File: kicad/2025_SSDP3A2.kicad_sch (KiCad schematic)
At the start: 72 parts, among them J1 SolderPad, J2 SolderPad, J3 SolderPad, J4 SolderPad, J5 SolderPad, J6 SolderPad, J7 SolderPad_01x02, J8 SolderPad_1x03, Q1 CSD19537Q3, Q2 CSD19537Q3, Q3 BSZ096N10LS5, U1 LM5050-1, U2 LM5146RGYR

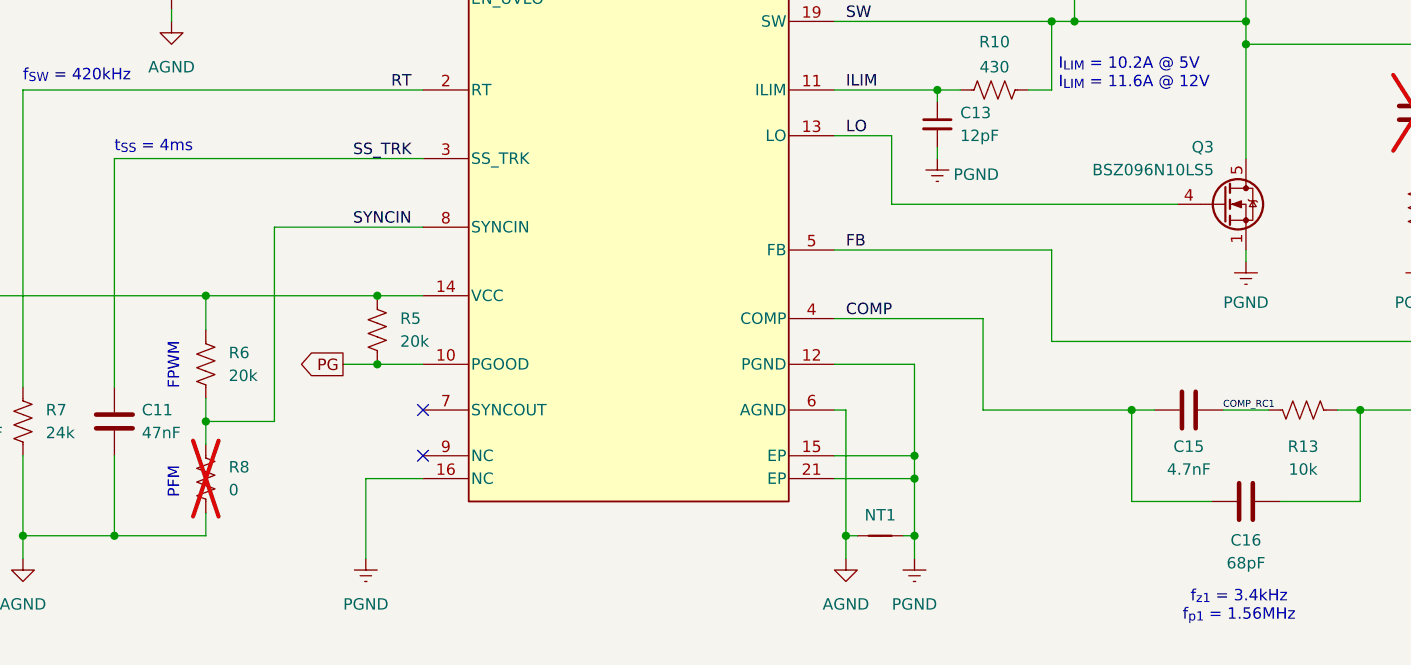
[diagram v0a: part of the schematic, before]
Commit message: Removed license-restricted files
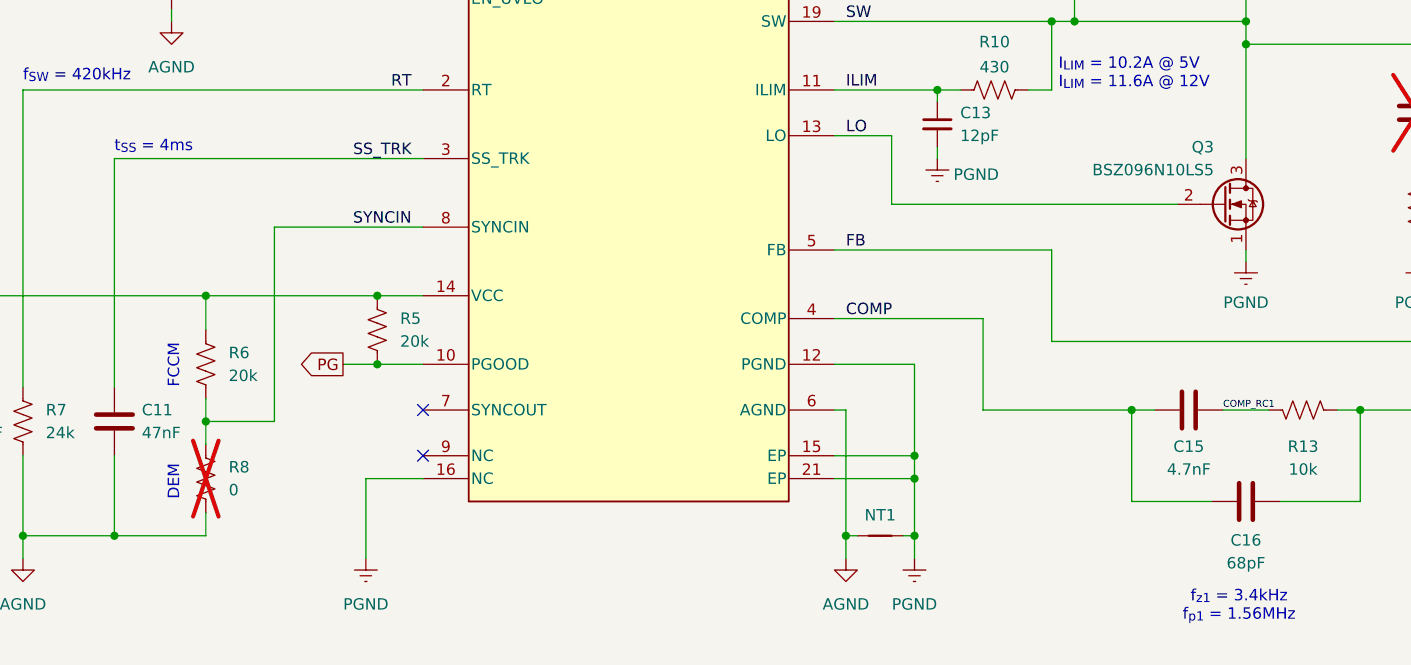
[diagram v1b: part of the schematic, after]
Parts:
- J7: footprint Connector_Custom:SolderWirePad_1x02_SMD_1.5x2mm -> Connector_Pad:SolderWirePad_1x02_SMD_1.5x2mm
- J8: footprint Connector_Custom:SolderWirePad_1x03_SMD_1.5x2mm -> Connector_Pad:SolderWirePad_1x03_SMD_1.5x2mm
- Q1, Q2: footprint Package_SON:VSON-8_3.3x3.3mm_P0.65mm_NexFET_THIN_TRACE -> Package_SON_JJ:Texas_DQG0008A_3.3x3.3mm_P0.65mm_ThermalVias-D0.3mm
- Q3: footprint TSDSON-8:PG-TSDSON-8-26 -> Package_SON_JJ:Infineon_PG-TSDSON-8-26_3.3x3.3mm_P0.65mm; symbol BSZ097N10LS5:BSC098N10NS5 -> Julian_Symbols:BSZ096N10LS5
- U2: symbol LM5146RGYR:LM5146RGYR -> Julian_Symbols:LM5146RGYR
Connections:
- net LO: now also Q3.2 (G); no longer Q3.4 (G)
- net PGND: no longer Q3.2 (S), Q3.3 (S)
- net SW: now also Q3.3 (D); no longer Q3.5 (D), Q3.6 (D), Q3.7 (D), Q3.8 (D)
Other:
- note added: "DEM"
- note added: "FCCM"
- note removed: "FPWM"
- note removed: "PFM"
- company: UBCO Aerospace Club [Julian Joaquin] -> UBCO Aerospace [Julian Joaquin]
- title: Super Step Down P3A2 -> Super Step Down V3
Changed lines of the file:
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@@
 	(paper "A3")
 	(title_block
-		(title "Super Step Down P3A2")
-		(date "2025-10-16")
+		(title "Super Step Down V3")
+		(date "2025-10-19")
 		(rev "C")
-		(company "UBCO Aerospace Club [Julian Joaquin]")
-		(comment 1 "An independent prototype design for the Super Step Down V3")
+		(company "UBCO Aerospace [Julian Joaquin]")
+		(comment 1 "A 12S battery eliminator circuit (BEC) for UAS applications.")
 	)
 	(rectangle
@@
 		)
 	)
-	(text "PFM"
+	(text "DEM"
 		(exclude_from_sim no)
 		(at 73.914 188.468 90)
@@
 		)
 	)
-	(text "FPWM"
+	(text "FCCM"
 		(exclude_from_sim no)
 		(at 73.914 175.514 90)
@@
 	)
 	(symbol
-		(lib_id "LM5146RGYR:LM5146RGYR")
+		(lib_id "Julian_Symbols:LM5146RGYR")
 		(at 101.6 124.46 0)
 		(unit 1)
@@
 			)
 		)
-		(property "Footprint" "Connector_Custom:SolderWirePad_1x03_SMD_1.5x2mm"
+		(property "Footprint" "Connector_Pad:SolderWirePad_1x03_SMD_1.5x2mm"
 			(at 361.95 232.41 0)
 			(effects
@@
 			)
 		)
-		(property "Footprint" "Package_SON:VSON-8_3.3x3.3mm_P0.65mm_NexFET_THIN_TRACE"
+		(property "Footprint" "Package_SON_JJ:Texas_DQG0008A_3.3x3.3mm_P0.65mm_ThermalVias-D0.3mm"
 			(at 195.58 126.365 0)
 			(effects
@@
 			)
 		)
-		(property "Footprint" "Package_SON:VSON-8_3.3x3.3mm_P0.65mm_NexFET_THIN_TRACE"
+		(property "Footprint" "Package_SON_JJ:Texas_DQG0008A_3.3x3.3mm_P0.65mm_ThermalVias-D0.3mm"
 			(at 156.845 30.48 0)
 			(effects
@@
 			)
 		)
-		(property "Footprint" "Connector_Custom:SolderWirePad_1x02_SMD_1.5x2mm"
+		(property "Footprint" "Connector_Pad:SolderWirePad_1x02_SMD_1.5x2mm"
 			(at 359.41 195.58 0)
 			(effects
@@
 	)
 	(symbol
-		(lib_id "BSZ097N10LS5:BSC098N10NS5")
+		(lib_id "Julian_Symbols:BSZ096N10LS5")
 		(at 190.5 157.48 0)
 		(unit 1)
@@
 			)
 		)
-		(property "Footprint" "TSDSON-8:PG-TSDSON-8-26"
+		(property "Footprint" "Package_SON_JJ:Infineon_PG-TSDSON-8-26_3.3x3.3mm_P0.65mm"
 			(at 195.58 159.385 0)
 			(effects
@@
 			)
 		)
-		(property "LCSC PN" "C534695"
+		(property "Part Number" "BSZ096N10LS5"
 			(at 190.5 157.48 0)
 			(effects
@@
 			)
 		)
-		(property "Part Type" "Extended"
+		(property "LCSC PN" "C534695"
 			(at 190.5 157.48 0)
 			(effects
@@
 			)
 		)
-		(property "ESR" "9.6mΩ"
+		(property "Part Type" "Extended"
 			(at 190.5 157.48 0)
 			(effects
@@
 			)
 		)
-		(property "Voltage" "100V"
+		(property "ESR" "9.6mΩ"
 			(at 190.5 157.48 0)
 			(effects
@@
 			)
 		)
-		(property "LCSC ALT1" "C534697"
+		(property "Voltage" "100V"
 			(at 190.5 157.48 0)
 			(effects
@@
 			)
 		)
-		(property "PART ALT1" "BSZ097N10NS5"
+		(property "LCSC ALT1" "C534697"
 			(at 190.5 157.48 0)
 			(effects
@@
 			)
 		)
-		(property "Part Number" "BSZ096N10LS5"
+		(property "PART ALT1" "BSZ097N10NS5"
 			(at 190.5 157.48 0)
 			(effects
@@
 		(pin "1"
 		)
-		(pin "5"
-		)
 		(pin "2"
 		)
-		(pin "4"
-		)
 		(pin "3"
 		)
-		(pin "8"
-		)
-		(pin "7"
-		)
-		(pin "6"
-		)
 		(instances
